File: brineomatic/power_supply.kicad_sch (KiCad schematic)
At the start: 27 parts, among them J10 5.08MM, J9 5.08MM, Q3 20N06, U2 LM74700, U3 XL1509-5.0

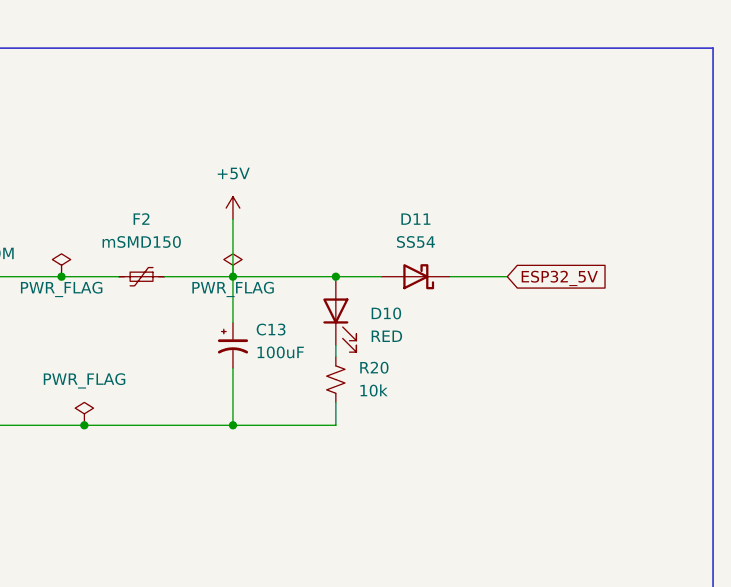
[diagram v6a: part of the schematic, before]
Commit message: changed mosfet pulldowns to 10k. moved 5v to esp32_5v to power everything over usb.
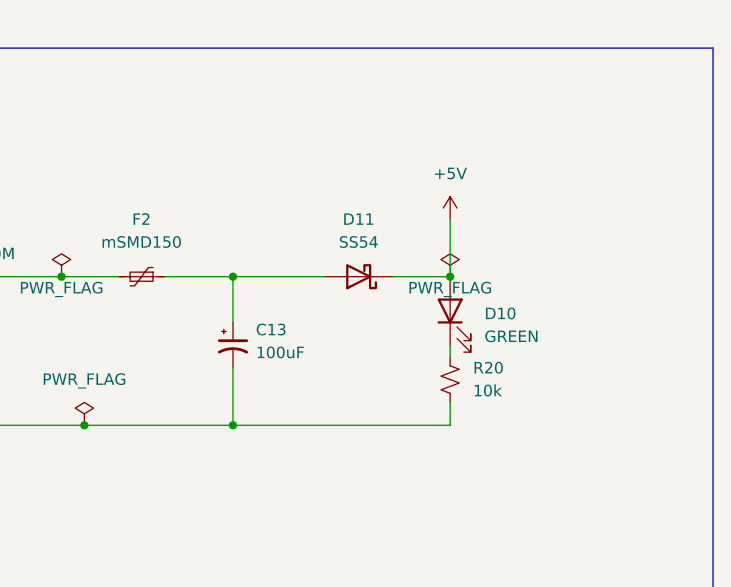
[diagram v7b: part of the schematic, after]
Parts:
- D10: value RED -> GREEN
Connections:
- net ESP32_5V is gone; now on net +5V: D11.1 (K)
- net +5V: no longer C13.1, D11.2 (A), F2.1
- new net: C13.1, D11.2 (A), F2.1
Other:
- moved on the sheet: D10, D11, R20
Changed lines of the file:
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@@
 	)
 	(junction
-		(at 231.14 120.65)
-		(diameter 0)
-		(color 0 0 0 0)
-	)
-	(junction
 		(at 200.66 120.65)
 		(diameter 0)
@@
 		(color 0 0 0 0)
 	)
+	(junction
+		(at 243.84 120.65)
+		(diameter 0)
+		(color 0 0 0 0)
+	)
 	(no_connect
 		(at 41.91 52.07)
@@
 	(wire
 		(pts
-			(xy 243.84 120.65) (xy 250.19 120.65)
+			(xy 237.49 120.65) (xy 243.84 120.65)
 		)
 		(stroke
@@
 	(wire
 		(pts
-			(xy 231.14 128.27) (xy 231.14 129.54)
+			(xy 243.84 128.27) (xy 243.84 129.54)
 		)
 		(stroke
@@
 	(wire
 		(pts
-			(xy 219.71 114.3) (xy 219.71 120.65)
+			(xy 243.84 114.3) (xy 243.84 120.65)
 		)
 		(stroke
@@
 	(wire
 		(pts
-			(xy 231.14 120.65) (xy 236.22 120.65)
-		)
-		(stroke
-			(width 0)
-			(type default)
-		)
-	)
-	(wire
-		(pts
 			(xy 106.68 120.65) (xy 118.11 120.65)
 		)
@@
 	(wire
 		(pts
-			(xy 219.71 120.65) (xy 231.14 120.65)
+			(xy 219.71 120.65) (xy 229.87 120.65)
 		)
 		(stroke
@@
 	(wire
 		(pts
-			(xy 219.71 137.16) (xy 231.14 137.16)
+			(xy 219.71 137.16) (xy 243.84 137.16)
 		)
 		(stroke
@@
 	(wire
 		(pts
-			(xy 231.14 134.62) (xy 231.14 137.16)
+			(xy 243.84 134.62) (xy 243.84 137.16)
 		)
 		(stroke
@@
 		)
 	)
-	(global_label "ESP32_5V"
-		(shape input)
-		(at 250.19 120.65 0)
-		(fields_autoplaced yes)
-		(effects
-			(font
-				(size 1.27 1.27)
-			)
-			(justify left)
-		)
-		(property "Intersheetrefs" "${INTERSHEET_REFS}"
-			(at 262.4884 120.65 0)
-			(effects
-				(font
-					(size 1.27 1.27)
-				)
-				(justify left)
-				(hide yes)
-			)
-		)
-	)
 	(symbol
 		(lib_id "power:GND")
@@
 	(symbol
 		(lib_id "power:PWR_FLAG")
-		(at 219.71 120.65 0)
-		(unit 1)
-		(exclude_from_sim no)
-		(in_bom yes)
-		(on_board yes)
-		(dnp no)
-		(property "Reference" "#FLG07"
-			(at 219.71 118.745 0)
-			(effects
-				(font
-					(size 1.27 1.27)
-				)
-				(hide yes)
-			)
-		)
-		(property "Value" "PWR_FLAG"
-			(at 219.71 121.92 0)
-			(effects
-				(font
-					(size 1.27 1.27)
-				)
-			)
-		)
-		(property "Footprint" ""
-			(at 219.71 120.65 0)
-			(effects
-				(font
-					(size 1.27 1.27)
-				)
-				(hide yes)
-			)
-		)
-		(property "Datasheet" "~"
-			(at 219.71 120.65 0)
-			(effects
-				(font
-					(size 1.27 1.27)
-				)
-				(hide yes)
-			)
-		)
-		(property "Description" "Special symbol for telling ERC where power comes from"
-			(at 219.71 120.65 0)
-			(effects
-				(font
-					(size 1.27 1.27)
-				)
-				(hide yes)
-			)
-		)
-		(pin "1"
-		)
-		(instances
-			(project "brineomatic"
-				(path "/96477ae2-ef08-48f3-8dd4-fe4478541f68/7cbb3b3c-cf93-4880-b816-c6df902b993c"
-					(reference "#FLG07")
-					(unit 1)
-				)
-			)
-		)
-	)
-	(symbol
-		(lib_id "power:PWR_FLAG")
 		(at 82.55 119.38 0)
 		(unit 1)
@@
 	(symbol
 		(lib_id "power:+5V")
-		(at 219.71 114.3 0)
+		(at 243.84 114.3 0)
 		(unit 1)
 		(exclude_from_sim no)
@@
 		(fields_autoplaced yes)
 		(property "Reference" "#PWR031"
-			(at 219.71 118.11 0)
+			(at 243.84 118.11 0)
 			(effects
 				(font
@@
 		)
 		(property "Value" "+5V"
-			(at 219.71 109.22 0)
+			(at 243.84 109.22 0)
 			(effects
 				(font
@@
 		)
 		(property "Footprint" ""
-			(at 219.71 114.3 0)
+			(at 243.84 114.3 0)
 			(effects
 				(font
@@
 		)
 		(property "Datasheet" ""
-			(at 219.71 114.3 0)
+			(at 243.84 114.3 0)
 			(effects
 				(font
@@
 		)
 		(property "Description" "Power symbol creates a global label with name \"+5V\""
-			(at 219.71 114.3 0)
+			(at 243.84 114.3 0)
 			(effects
 				(font
@@
 	(symbol
 		(lib_id "Device:D_Schottky")
-		(at 240.03 120.65 180)
+		(at 233.68 120.65 180)
 		(unit 1)
 		(exclude_from_sim no)
@@
 		(fields_autoplaced yes)
 		(property "Reference" "D11"
-			(at 240.03 114.3 0)
+			(at 233.68 114.3 0)
 			(effects
 				(font
@@
 		)
 		(property "Value" "SS54"
-			(at 240.03 116.84 0)
+			(at 233.68 116.84 0)
 			(effects
 				(font
@@
 		)
 		(property "Footprint" "Diode_SMD:D_SMA"
-			(at 240.03 120.65 0)
+			(at 233.68 120.65 0)
 			(effects
 				(font
@@
 		)
 		(property "Datasheet" "~"
-			(at 240.03 120.65 0)
+			(at 233.68 120.65 0)
 			(effects
 				(font
@@
 		)
 		(property "Description" ""
-			(at 240.03 120.65 0)
+			(at 233.68 120.65 0)
 			(effects
 				(font
@@
 		)
 		(property "Mouser" ""
-			(at 240.03 120.65 90)
+			(at 233.68 120.65 90)
 			(effects
 				(font
@@
 		)
 		(property "LCSC" "C22452"
-			(at 240.03 120.65 0)
+			(at 233.68 120.65 0)
 			(effects
 				(font
@@
 	)
 	(symbol
+		(lib_id "power:PWR_FLAG")
+		(at 243.84 120.65 0)
+		(unit 1)
+		(exclude_from_sim no)
+		(in_bom yes)
+		(on_board yes)
+		(dnp no)
+		(property "Reference" "#FLG010"
+			(at 243.84 118.745 0)
+			(effects
+				(font
+					(size 1.27 1.27)
+				)
+				(hide yes)
+			)
+		)
+		(property "Value" "PWR_FLAG"
+			(at 243.84 121.92 0)
+			(effects
+				(font
+					(size 1.27 1.27)
+				)
+			)
+		)
+		(property "Footprint" ""
+			(at 243.84 120.65 0)
+			(effects
+				(font
+					(size 1.27 1.27)
+				)
+				(hide yes)
+			)
+		)
+		(property "Datasheet" "~"
+			(at 243.84 120.65 0)
+			(effects
+				(font
+					(size 1.27 1.27)
+				)
+				(hide yes)
+			)
+		)
+		(property "Description" "Special symbol for telling ERC where power comes from"
+			(at 243.84 120.65 0)
+			(effects
+				(font
+					(size 1.27 1.27)
+				)
+				(hide yes)
+			)
+		)
+		(pin "1"
+		)
+		(instances
+			(project "brineomatic"
+				(path "/96477ae2-ef08-48f3-8dd4-fe4478541f68/7cbb3b3c-cf93-4880-b816-c6df902b993c"
+					(reference "#FLG010")
+					(unit 1)
+				)
+			)
+		)
+	)
+	(symbol
 		(lib_id "power:+24V")
 		(at 52.07 115.57 0)
@@
 	(symbol
 		(lib_id "Device:R_Small_US")
-		(at 231.14 132.08 0)
+		(at 243.84 132.08 0)
 		(unit 1)
 		(exclude_from_sim no)
@@
 		(fields_autoplaced yes)
 		(property "Reference" "R20"
-			(at 233.68 130.8099 0)
+			(at 246.38 130.8099 0)
 			(effects
 				(font
@@
 		)
 		(property "Value" "10k"
-			(at 233.68 133.3499 0)
+			(at 246.38 133.3499 0)
 			(effects
 				(font
@@
 		)
 		(property "Footprint" "Resistor_SMD:R_0603_1608Metric"
-			(at 231.14 132.08 0)
+			(at 243.84 132.08 0)
 			(effects
 				(font
@@
 		)
 		(property "Datasheet" "~"
-			(at 231.14 132.08 0)
+			(at 243.84 132.08 0)
 			(effects
 				(font
@@
 		)
 		(property "Description" "Resistor, small US symbol"
-			(at 231.14 132.08 0)
+			(at 243.84 132.08 0)
 			(effects
 				(font
@@
 	(symbol
 		(lib_id "Device:LED")
-		(at 231.14 124.46 90)
+		(at 243.84 124.46 90)
 		(unit 1)
 		(exclude_from_sim no)
@@
 		(fields_autoplaced yes)
 		(property "Reference" "D10"
-			(at 234.95 124.7774 90)
+			(at 247.65 124.7774 90)
 			(effects
 				(font
@@
 			)
 		)
-		(property "Value" "RED"
-			(at 234.95 127.3174 90)
+		(property "Value" "GREEN"
+			(at 247.65 127.3174 90)
 			(effects
 				(font
@@
 		)
 		(property "Footprint" "LED_SMD:LED_0603_1608Metric"
-			(at 231.14 124.46 0)
+			(at 243.84 124.46 0)
 			(effects
 				(font
@@
 		)
 		(property "Datasheet" "~"
-			(at 231.14 124.46 0)
+			(at 243.84 124.46 0)
 			(effects
 				(font
@@
 		)
 		(property "Description" "Light emitting diode"
-			(at 231.14 124.46 0)
+			(at 243.84 124.46 0)
 			(effects
 				(font
@@
 		)
 		(property "Sim.Pins" "1=K 2=A"
-			(at 231.14 124.46 0)
+			(at 243.84 124.46 0)
 			(effects
 				(font
@@
 		)
 		(property "LCSC" "C965799"
-			(at 231.14 124.46 90)
+			(at 243.84 124.46 90)
 			(effects
 				(font

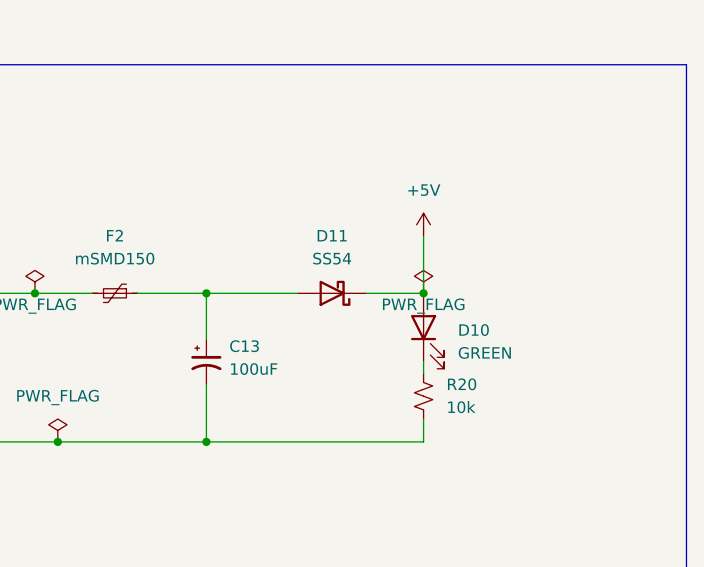
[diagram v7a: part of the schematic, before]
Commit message: added rs485 circuit
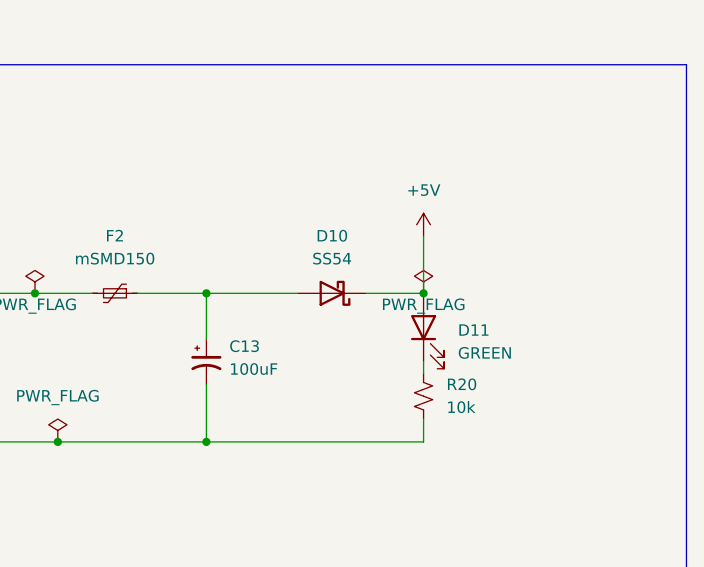
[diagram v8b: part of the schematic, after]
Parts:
- renumbered D11 to D10, D10 to D11
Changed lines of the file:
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@@
 		(dnp no)
 		(fields_autoplaced yes)
-		(property "Reference" "D11"
+		(property "Reference" "D10"
 			(at 233.68 114.3 0)
 			(effects
@@
 			(project "brineomatic"
 				(path "/96477ae2-ef08-48f3-8dd4-fe4478541f68/7cbb3b3c-cf93-4880-b816-c6df902b993c"
-					(reference "D11")
+					(reference "D10")
 					(unit 1)
 				)
@@
 		(on_board yes)
 		(dnp no)
-		(property "Reference" "#FLG010"
+		(property "Reference" "#FLG07"
 			(at 243.84 118.745 0)
 			(effects
@@
 			(project "brineomatic"
 				(path "/96477ae2-ef08-48f3-8dd4-fe4478541f68/7cbb3b3c-cf93-4880-b816-c6df902b993c"
-					(reference "#FLG010")
+					(reference "#FLG07")
 					(unit 1)
 				)
@@
 		(dnp no)
 		(fields_autoplaced yes)
-		(property "Reference" "D10"
+		(property "Reference" "D11"
 			(at 247.65 124.7774 90)
 			(effects
@@
 			(project "brineomatic"
 				(path "/96477ae2-ef08-48f3-8dd4-fe4478541f68/7cbb3b3c-cf93-4880-b816-c6df902b993c"
-					(reference "D10")
-					(unit 1)
-				)
+					(reference "D11")
+					(unit 1)
+				)
